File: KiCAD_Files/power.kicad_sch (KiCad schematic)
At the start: 145 parts, among them J1 Conn_01x01, J2 Conn_01x01, J3 Conn_01x01, J5 Conn_01x01, J8 Conn_01x01, K1 HF140FF/012-2HSWTF, Q1 CID12N65D, Q10 CJAC90SN12, Q11 ZXMN7A11GTA, Q2 CID12N65D, Q3 CID12N65D, Q4 CID12N65D, Q5 CJAC90SN12, Q6 CJAC90SN12, Q7 CJAC90SN12, Q8 CJAC90SN12, Q9 CJAC90SN12, T1 Transformer_1P_1S, T2 Transformer_1P_1S, U1 INA240A1PW, U2 INA240A1PWR, U3 UCC27282DRC, U4 UCC27282DRC

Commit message: Added passive references. Added ESD protection for MCU pins.
Signed-off-by: Jean Alinei <jean.alinei@owntech.org>
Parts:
- added C122: 120nF, Capacitor_THT:C_Rect_L13.0mm_W6.0mm_P10.00mm_FKS3_FKP3_MKS4, symbol Device:C_Small
- added C123, C124: 2.2nF, Capacitor_THT:C_Rect_L10.3mm_W4.5mm_P7.50mm_MKS4, symbol Device:C_Small
- added C125, C126: 1nF, Capacitor_THT:C_Rect_L10.3mm_W4.5mm_P7.50mm_MKS4, symbol Device:C_Small
- C1, C12, C14, C3: value C_Small -> 1uF; LCSC (none) -> C28323
- C10, C116, C117, C5: value 2.2nF -> 4.7nF; footprint Capacitor_THT:C_Rect_L9.0mm_W4.0mm_P7.50mm_MKT -> Capacitor_THT:C_Rect_L13.0mm_W6.0mm_P10.00mm_FKS3_FKP3_MKS4; LCSC C5121878 -> C328768
- C101, C102: LCSC (none) -> C1779
- C103, C110, C18, C25, C34: value 10µF -> 4.7uF; LCSC C5449000 -> C22367839
- C104, C105, C106, C107, C108, C109, C19, C20, C21, C23, C24, C26, C29, C30, C32, C35, C36, C37: value C -> 4.7uF; LCSC C5449000 -> C22367839
- C11, C54, Logo101, T1, T2: now not fitted
- C111: Rotation Offset (none) -> 180
- C112: value 47uH -> 47uF; Rotation Offset (none) -> 180
- C113: value ?nF -> 120nF; footprint Capacitor_THT:C_Rect_L16.5mm_W7.0mm_P15.00mm_MKT -> Capacitor_THT:C_Rect_L13.0mm_W6.0mm_P10.00mm_FKS3_FKP3_MKS4; LCSC C489081 -> C46638860
- C114, C115, C16, C17: value 1nF -> 100nF; Dielectric X7R -> (none); LCSC (none) -> C22374890; Package 1210 -> (none); Subfunction Decoupling Capacitor -> (none); VRating 600V -> (none); Voltage 200V -> (none); Voltage_Rating (none) -> 600V; manf# C1206C103K2RAC -> (none)
- C120: footprint Capacitor_THT:C_Rect_L9.0mm_W4.0mm_P7.50mm_MKT -> Capacitor_THT:C_Rect_L10.3mm_W4.5mm_P7.50mm_MKS4; LCSC C489081 -> C47278939
- C13, C15: value C_Small -> 4.7uF; LCSC (none) -> C1779
- C22, C27, C33, C38: value 680nF -> 1uF; footprint Footprints:C_Rect_L16.5mm_W8mm_P15.00mm_MKT -> Capacitor_THT:C_Rect_L16.5mm_W8.7mm_P15.00mm_MKT; LCSC C7529558 -> C7529557
- C28, C39: LCSC (none) -> C49678
- C31: value 10 µF -> 4.7uF; LCSC C5449000 -> C22367839
- C40, C53, C8, C9: LCSC (none) -> C1623
- C6: LCSC C783662 -> (none); now not fitted
- D1, D2, D3, D4: Position Offset (none) -> -1.85,0; Rotation Offset (none) -> 180
- D101, D102: value D -> ES1JW; LCSC (none) -> C108815
- FL3: LCSC C30584795 -> C2997440
- L1, L3: value 330uH -> 250uH
- L5, L6, Q1, Q2, Q3, Q4: Rotation Offset (none) -> 90
- R1, R2, R4, R5: value R_Small -> 33; LCSC (none) -> C17634
- R101, R109, R32, R33, R8: LCSC (none) -> C4184
- R102, R103: LCSC (none) -> C16257
- R104, R105, R106, R107, R108: LCSC (none) -> C22950
- R110: renamed from R6; LCSC (none) -> C25804
- R12: LCSC (none) -> C17729
- R13: LCSC (none) -> C17414
- R9: LCSC (none) -> C25804
- U1: value INA240A1PW -> INA240A1PWR
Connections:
- net AC Current sense/In+: now also C125.2
- net Earth_Protective: now also C123.1, C124.2, C125.1, C126.2
- net Grid Voltage sense/In+: now also C122.1, C126.1
- net HV_{BUS}: no longer Q1.4, Q2.4
- net Neut_{REF}: now also C122.2
- net SN1: no longer Q3.4
- net SN2: no longer Q4.4
- net at C120.1, C7.1, FL1.1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: now also C124.1
- net at C120.2, FL1.4, L3.2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: now also C123.2
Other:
- sheet AC Current sense ports: added Vref; removed none
- sheet Grid Voltage sense ports: added Vref; removed none
- note added: "Thermal connections to chassis. Plain copper standoffs"
- moved on the sheet: C10, C113, C114, C115, C120, C13, C15, C16, C17, C5, C7, F1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

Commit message: Added TL431 for AC measurement 5V regulation. Added more film capacitance. Increased size of 100V ceramic caps to 1210.
Signed-off-by: Jean Alinei <jean.alinei@owntech.org>
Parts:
- added C127: 1uF, Capacitor_THT:C_Rect_L18.0mm_W8.0mm_P15.00mm_FKS3_FKP3, symbol Device:C_Small
- added C128, C129, C130, C131, C132, C133, C134, C135: 4.7uF, Footprints:C_1210_3225Metric, symbol Device:C
- C103, C104, C105, C106, C107, C108, C109, C110, C18, C19, C20, C21, C23, C24, C25, C26, C29, C30, C31, C32, C34, C35, C36, C37: footprint Capacitor_SMD:C_1206_3216Metric -> Footprints:C_1210_3225Metric; LCSC C22367839 -> C381466
- C118, C119: footprint Footprints:CAP-TH_L6.3-W4.4-P10.00-D0.6-S3.8 -> Footprints:C_TH_L6.3-W4.4-P10.00-D0.6-S3.8
- C121: value 680nF -> 1uF; footprint Capacitor_THT:C_Rect_L16.5mm_W8.7mm_P15.00mm_MKT -> Capacitor_THT:C_Rect_L18.0mm_W8.0mm_P15.00mm_FKS3_FKP3; LCSC C489081 -> C7529557
- C22, C27, C33, C38: footprint Capacitor_THT:C_Rect_L16.5mm_W8.7mm_P15.00mm_MKT -> Capacitor_THT:C_Rect_L18.0mm_W8.0mm_P15.00mm_FKS3_FKP3
- C6: footprint Footprints:film_capacitors -> Footprints:C_film_capacitors_board; now fitted
- C7: footprint Capacitor_THT:C_Rect_L16.5mm_W8.7mm_P15.00mm_MKT -> Capacitor_THT:C_Rect_L18.0mm_W9.0mm_P15.00mm_FKS3_FKP3
- D1, D2, D3, D4: footprint Footprints:Diode_TO-252-2 -> Footprints:TO-252-2_Diode
- FL1, FL2: footprint Footprints:FILTER-TH_XRSQ1515-5MH-V-1013 -> Footprints:Choke_TH_XRSQ1515-5MH-V-1013
- FL3: footprint Footprints:IND-TH_4P-L23.0-W15.0-P7.50-D1.0-S9.0 -> Footprints:Choke_TH_4P-L23.0-W15.0-P7.50-D1.0-S9.0
- HS101, HS104, HS105, HS106, HS107, HS108, HS109, HS11, HS110, HS111, HS12, HS5: footprint Footprints:BTC-533-ZN01 -> Footprints:Heatsink_BTC-533-ZN01
- J1, J2, J3, J5, J8: footprint Footprints:SMD-4_TS34056055-0440 -> Footprints:Connector_SMD-4_TS34056055-0440; symbol Connector_Generic:Conn_01x01 -> Symbols:Conn_01x01
- L1, L3: footprint Footprints:IND-SMD_L27.0-W19.5-LS23.5_60B104C -> Footprints:L_SMD_L27.0-W19.5-LS23.5_60B104C
- L5, L6: footprint Footprints:SRP1510CA-330M -> Footprints:L_SRP1510CA-330M
- R12, R13: footprint Capacitor_SMD:C_0805_2012Metric -> Resistor_SMD:R_0805_2012Metric
- T1, T2: now fitted
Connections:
- net GND_{HV}: now also C127.2
- net GND_{LV}: now also C130.2, C131.2, C132.2, C133.2
- net HV_{BUS}: now also C127.1
- net LSW3: now also C128.2, C129.2, C130.1, C131.1
- net LSW4: now also C132.1, C133.1, C134.2, C135.2
- net V_{IHigh1}: now also C134.1, C135.1
- net V_{IHigh2}: now also C128.1, C129.1
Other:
- moved on the sheet: C103, C104, C105, C106, C107, C108, C109, C110, C111, C112, C121, C18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

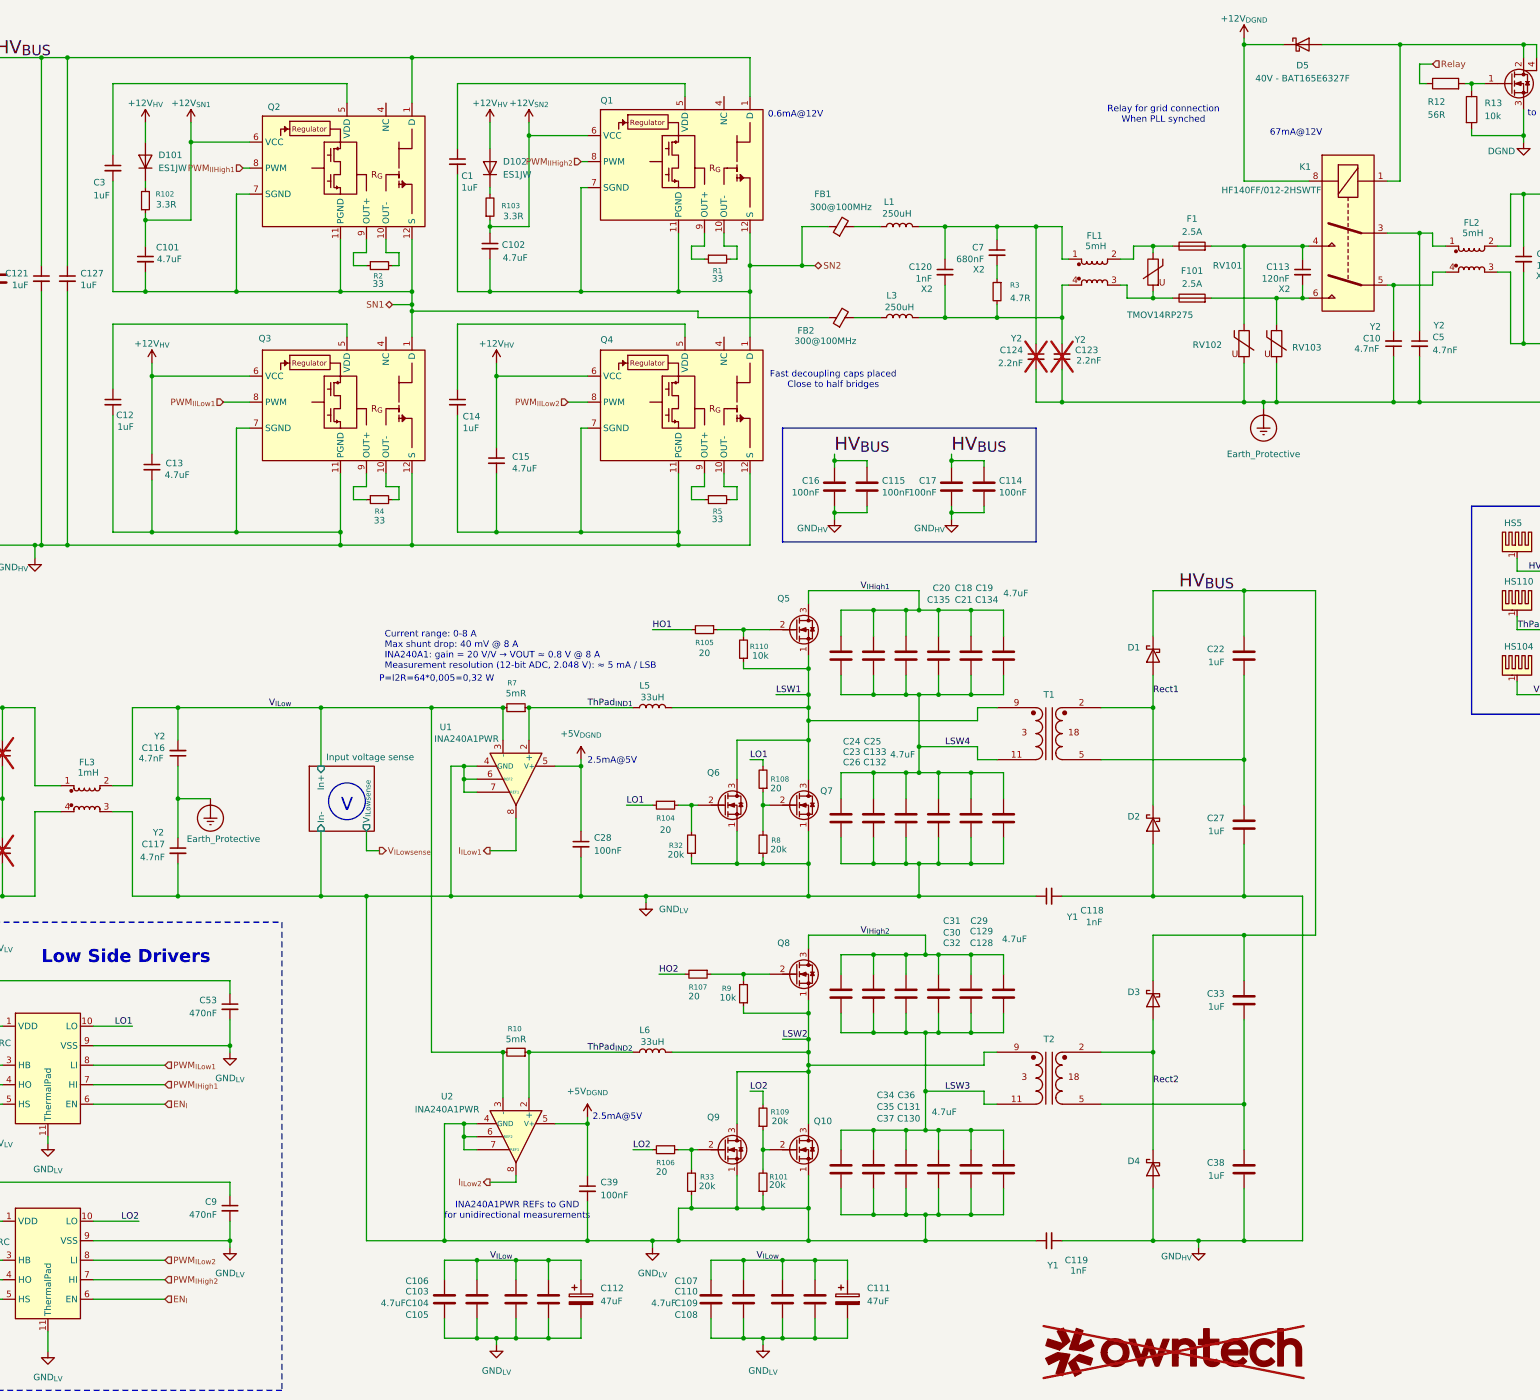
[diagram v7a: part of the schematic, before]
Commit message: V0.9 as ordered 23/01/26. Improved silkscreen, added 1nF on enable pin signals.
Signed-off-by: Jean Alinei <jean.alinei@owntech.org>
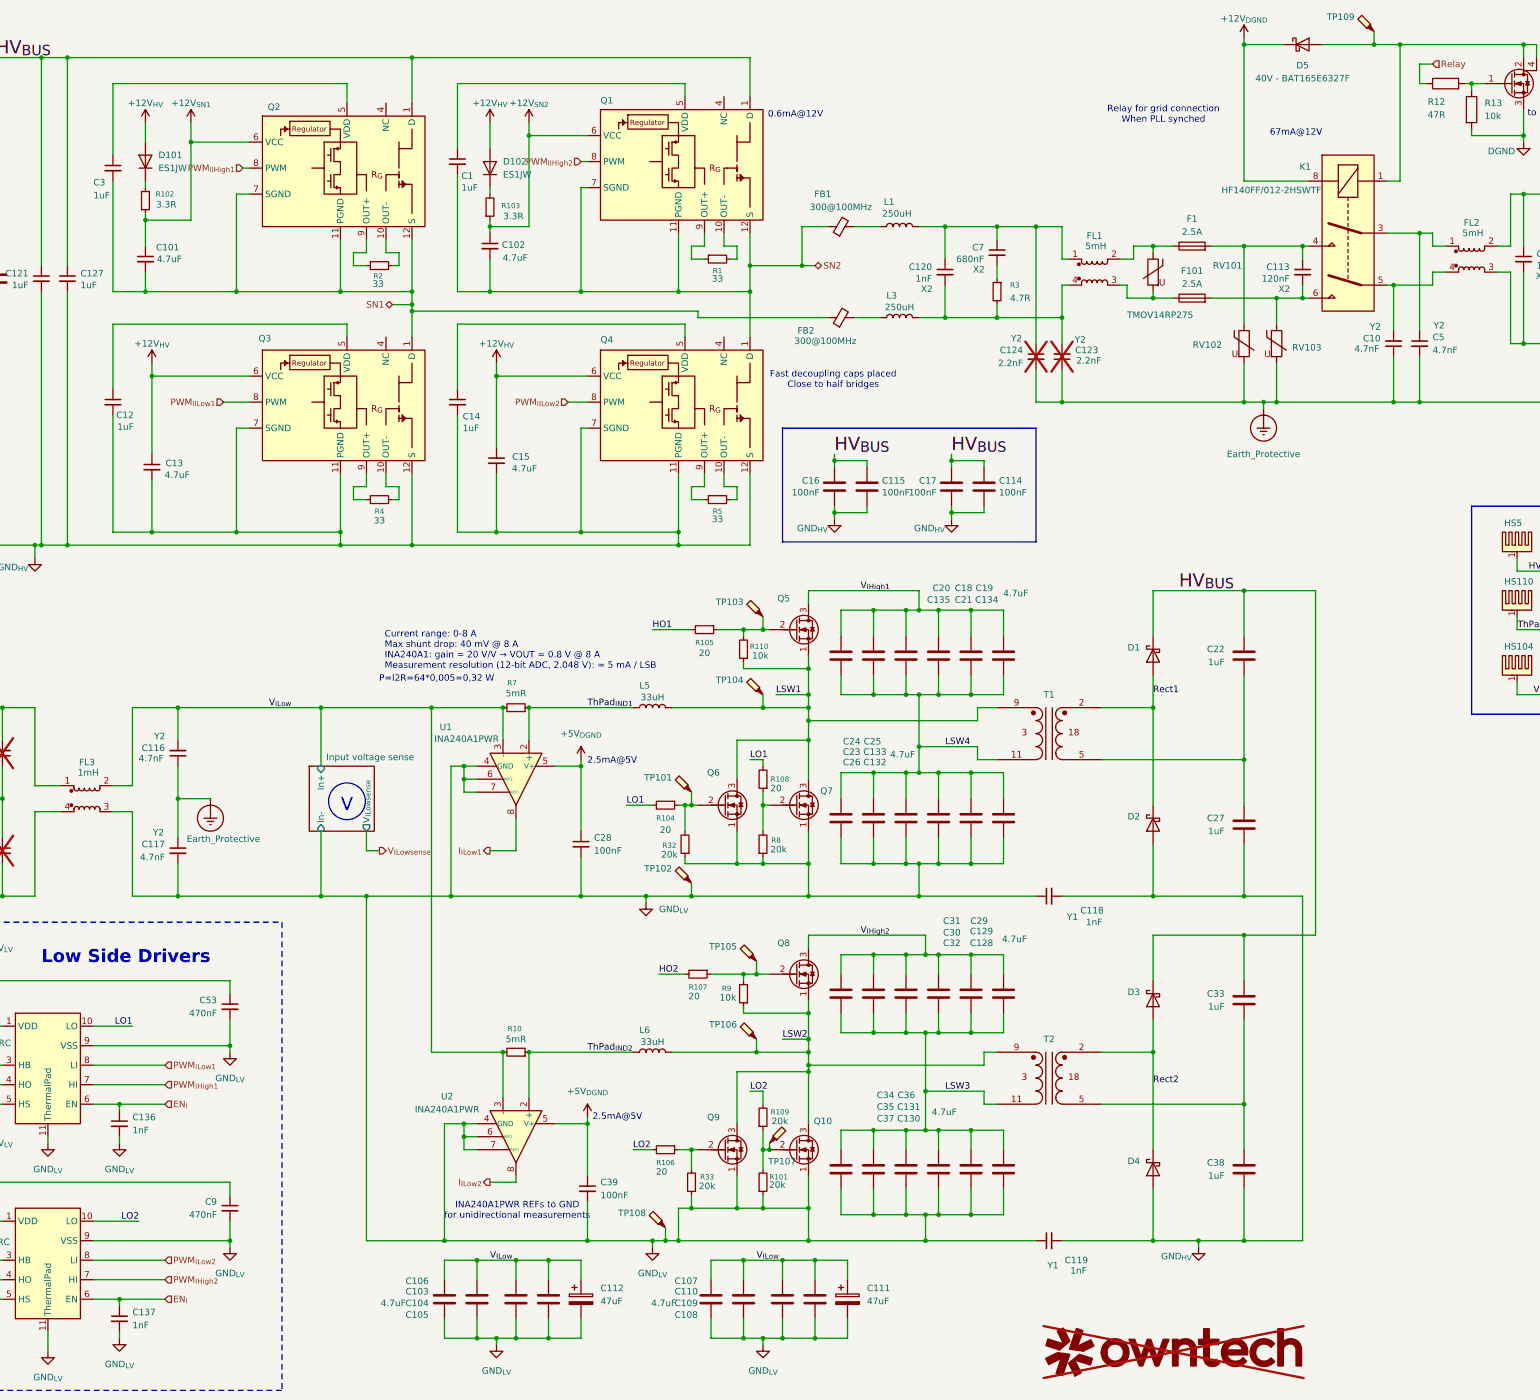
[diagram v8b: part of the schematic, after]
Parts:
- added C136, C137: 1nF, Capacitor_SMD:C_0603_1608Metric, symbol Device:C_Small
- added TP101, TP102, TP103, TP104, TP105, TP106, TP107, TP108, TP109: TestPoint_Probe, TestPoint:TestPoint_Pad_D1.0mm, symbol Connector:TestPoint_Probe
- R12: value 56R -> 47R; LCSC C17729 -> C17714
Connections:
- net EN_{I}: now also C136.1, C137.1
- net GND_{LV}: now also C136.2, C137.2, TP102.1, TP108.1
- net LSW1: now also TP104.1
- net LSW2: now also TP106.1
- net at D5.2 (A), K1.1, Q11.2 (D)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: now also TP109.1
- net at Q6.2 (G), R104.1, R32.2: now also TP101.1
- net at Q8.2 (G), R107.1, R9.2: now also TP105.1
- net at Q10.2 (G), R101.2, R109.1: now also TP107.1
- net at Q5.2 (G), R105.1, R110.2: now also TP103.1
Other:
- moved on the sheet: R32
